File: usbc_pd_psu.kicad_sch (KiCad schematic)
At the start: 35 parts, among them J1 USB-C 5 A, J2 OUTPUT, J3 PROG, Q1 AON6324, Q2 AON6324, Q3 AON6324, Q4 AON6324, Q5 TIP120, U1 CH224K, U2 IR2104, U3 IR2104, U4 LM358, U5 LP2950-5.0, U6 CH32V003F4P6

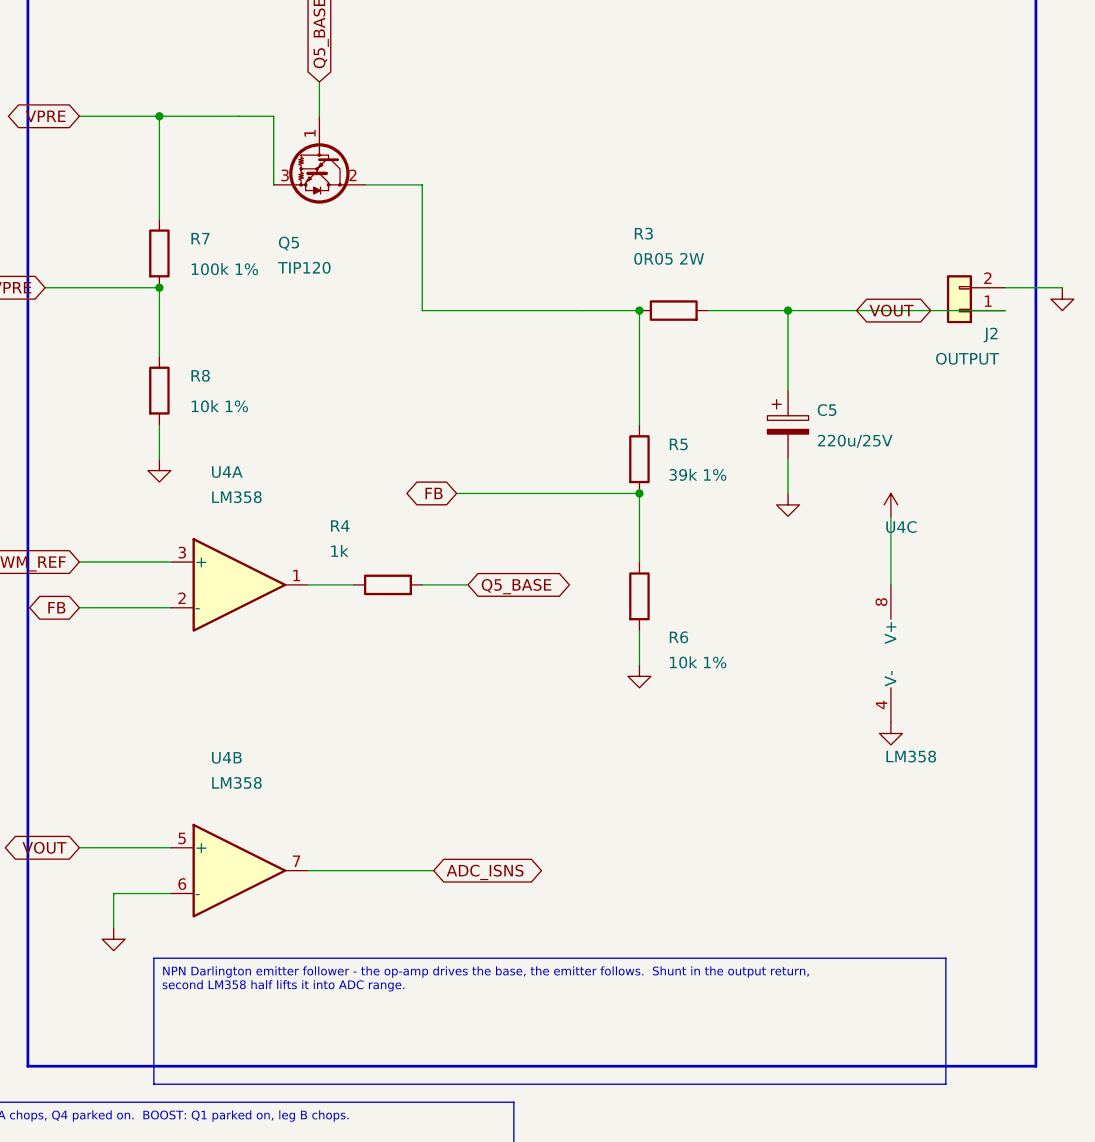
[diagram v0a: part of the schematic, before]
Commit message: v0.4: turn the pass device round to a PNP
The NPN follower cannot reach the top of the range.  Its base has to sit two
Vbe above the output, and the op-amp driving it runs from the same
pre-regulator rail as the pass device itself, so once the output climbs the
amplifier saturates before the base gets high enough.  The supply simply
stops following the setpoint near full scale.

Turning the device round fixes it: a TIP127 PNP Darlington SINKS base current
instead of sourcing it, so the stage needs no headroom above VOUT at all and
the pre-regulator only has to stay a dropout above the output.

Everything else on the sheet is unchanged - same MCU, same buck-boost, same
shunt in the output return.
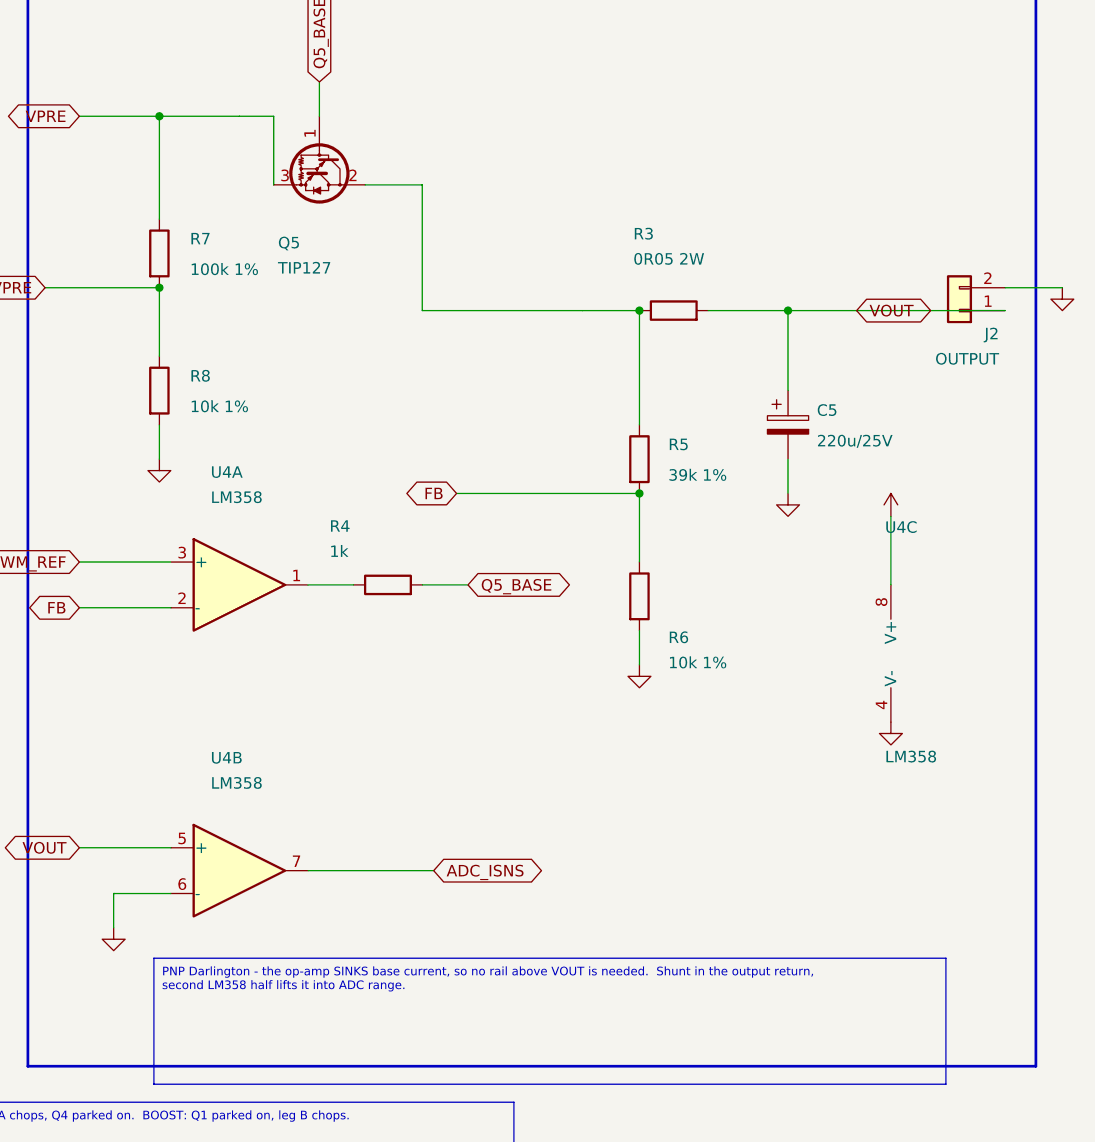
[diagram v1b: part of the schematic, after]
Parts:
- removed Q5: TIP120, Package_TO_SOT_THT:TO-220-3_Vertical, symbol Transistor_BJT:TIP120
- added Q5: TIP127, Package_TO_SOT_THT:TO-220-3_Vertical, symbol Transistor_BJT:TIP127
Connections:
- net Q5_BASE: now also Q5.1 (B)
- net VPRE: now also Q5.3 (E)
- net at R3.1, R5.1: now also Q5.2 (C)

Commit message: v0.5: add the front panel, and the MCU it needs
OLED, rotary encoder with its push, three keys and three indicator lamps.

Adding the panel needs eleven more pins and only two were left, so the MCU
moves up to a CH32V203C8T6.  Same RISC-V family, same toolchain, same
programming header - forty-eight pins instead of twenty, of which thirty-seven
are usable.  Nothing else on the sheet changes.

Choosing within the family rather than switching vendor keeps the existing
firmware work and the WCH-LinkE probe usable, which matters more at this stage
than the price difference.
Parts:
- removed U6: CH32V003F4P6, Package_SO:TSSOP-20_4.4x6.5mm_P0.65mm, symbol MCU_WCH_CH32V0:CH32V003FxPx
- added C9: 100nF, Capacitor_SMD:C_0805_2012Metric, symbol Device:C
- added D4: red, LED_SMD:LED_0805_2012Metric, symbol Device:LED
- added D5: amber, LED_SMD:LED_0805_2012Metric, symbol Device:LED
- added D6: green, LED_SMD:LED_0805_2012Metric, symbol Device:LED
- added J4: OLED 0.96in I2C, Connector_PinHeader_2.54mm:PinHeader_1x04_P2.54mm_Vertical, symbol Connector_Generic:Conn_01x04
- added R10, R9: 10k, Resistor_SMD:R_0805_2012Metric, symbol Device:R
- added R11, R12, R13: 1k, Resistor_SMD:R_0805_2012Metric, symbol Device:R
- added SW1: EC11, Rotary_Encoder:RotaryEncoder_Alps_EC11E-Switch_Vertical_H20mm, symbol Device:RotaryEncoder_Switch
- added SW2: OUTPUT, Button_Switch_SMD:SW_SPST_B3S-1000, symbol Switch:SW_Push
- added SW3: SELECT, Button_Switch_SMD:SW_SPST_B3S-1000, symbol Switch:SW_Push
- added SW4: BACK, Button_Switch_SMD:SW_SPST_B3S-1000, symbol Switch:SW_Push
- added U6: CH32V203C8T6, Package_QFP:LQFP-48_7x7mm_P0.5mm, symbol MCU_WCH_CH32V2:CH32V203CxTx
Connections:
- net +5V: now also C9.2, D4.2 (A), D5.2 (A), D6.2 (A), J4.1 (Pin_1), J4.2 (Pin_2), R10.2, R9.1, SW1.C, SW1.S2, SW2.1, SW3.1, SW4.1, U6.1 (VBAT), U6.23 (VSS), U6.24 (VDD_VIO), U6.35 (VSS), U6.36 (VDD), U6.47 (VSS), U6.48 (VDD), U6.8 (VSSA), U6.9 (VDDA)
- net ADC_ISNS: now also U6.14 (PA4)
- net ADC_VBUS: now also U6.10 (PA0)
- net ADC_VPRE: now also U6.11 (PA1)
- net CFG1: now also U6.20 (PB2)
- net CFG2: now also U6.21 (PB10)
- net CFG3: now also U6.22 (PB11)
- net EN_A: now also U6.31 (PA10)
- net EN_B: now also U6.32 (PA11)
- net PD_PG: now also U6.19 (PB1)
- net PWM_A: now also U6.29 (PA8)
- net PWM_B: now also U6.30 (PA9)
- net PWM_REF: now also U6.15 (PA5)
- net UART_RX: now also U6.43 (PB7); no longer J3.3 (Pin_3)
- net UART_TX: now also J3.3 (Pin_3), U6.42 (PB6); no longer J3.2 (Pin_2)
- net SWIO renamed SWDIO
- net SWDIO: now also U6.34 (SWDIO)
- new net: R10.1, U6.44 (BOOT0)
- new net: D6.1 (K), R13.1
- new net: C9.1, R9.2, U6.7 (~{RST})
- new net: D4.1 (K), R11.1
- new net: D5.1 (K), R12.1
- new net BTN_BACK: SW4.2, U6.4 (PC15)
- new net BTN_OUT: SW2.2, U6.2 (PC13)
- new net BTN_SEL: SW3.2, U6.3 (PC14)
- new net ENC_A: SW1.A, U6.25 (PB12)
- new net ENC_B: SW1.B, U6.26 (PB13)
- new net ENC_SW: SW1.S1, U6.27 (PB14)
- new net I2C_SCL: J4.3 (Pin_3), U6.45 (PB8)
- new net I2C_SDA: J4.4 (Pin_4), U6.46 (PB9)
- new net LED_CC: R12.2, U6.39 (PB3)
- new net LED_HB: R13.2, U6.40 (PB4)
- new net LED_OUT: R11.2, U6.38 (PA15)
- new net SWCLK: J3.2 (Pin_2), U6.37 (SWCLK)
- no-connect marks 4 -> 12
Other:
- note added: "7 - USER INTERFACE"

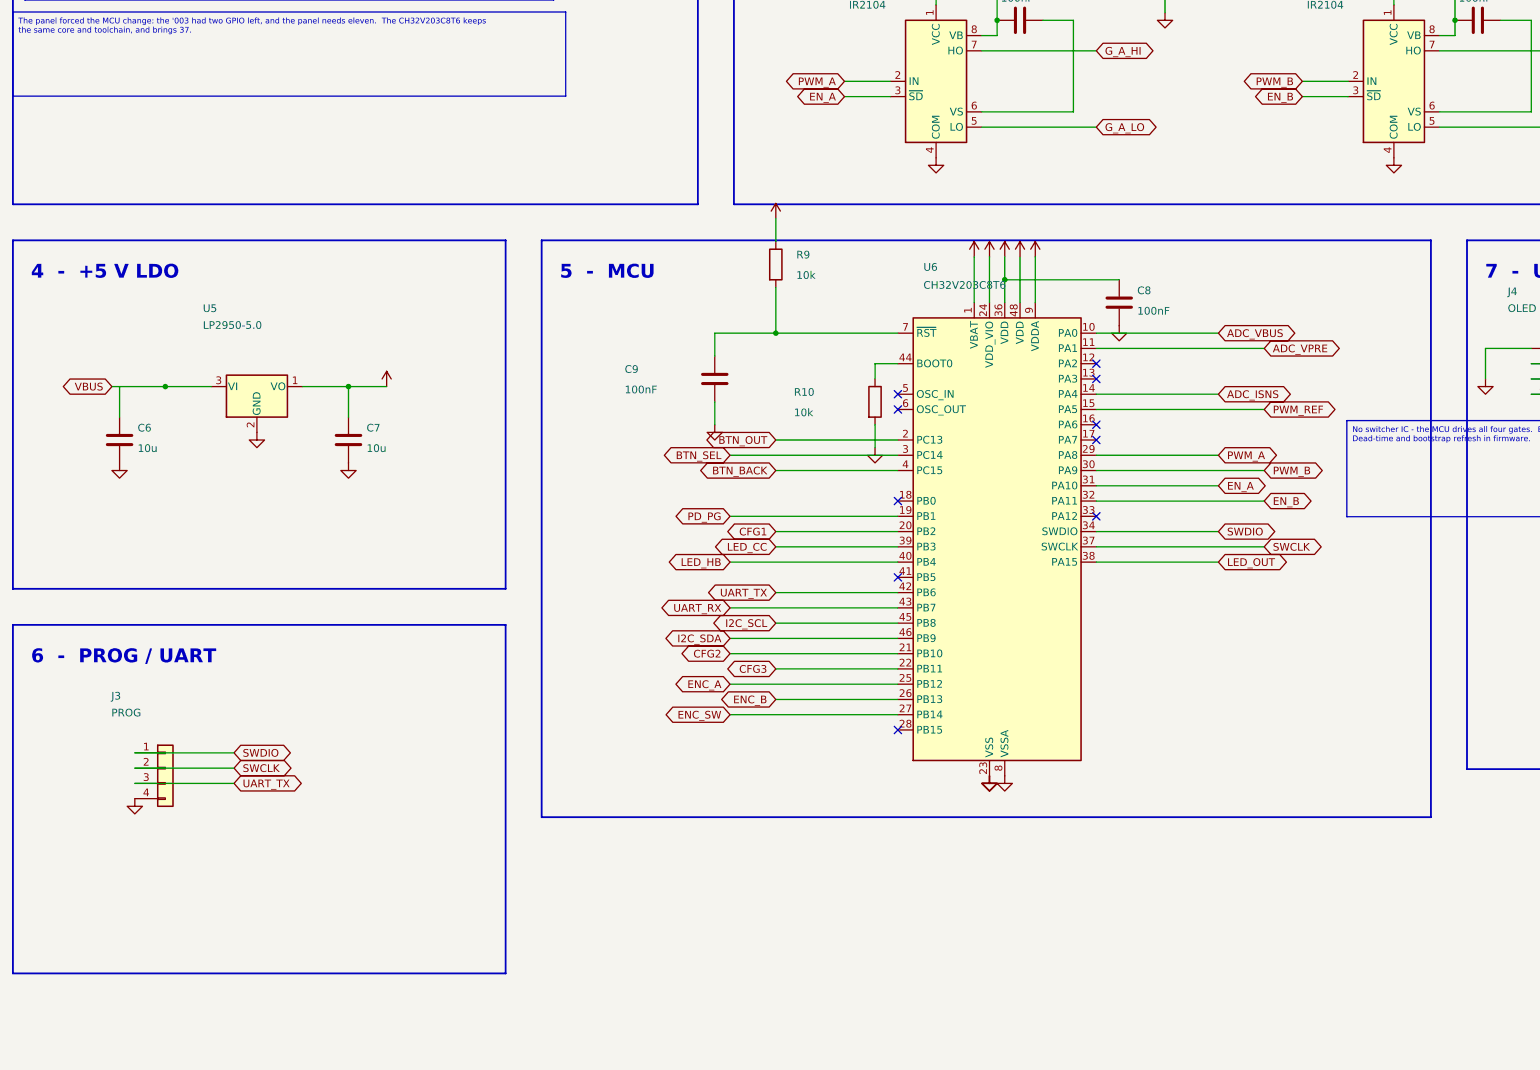
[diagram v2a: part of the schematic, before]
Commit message: v0.6: hardware over-current trip
A comparator watches the sense amplifier and pulls the driver enable low
directly.

Bench testing with a deliberate short showed the firmware loop cannot react in
time: by the time a 5 kHz loop notices, the FETs have already taken the
current.  The trip has to be hardware, and it has to bypass the MCU entirely.

This is also where the single-sheet layout runs out of room.  Everything still
fits, but only just, and the next thing added will not.
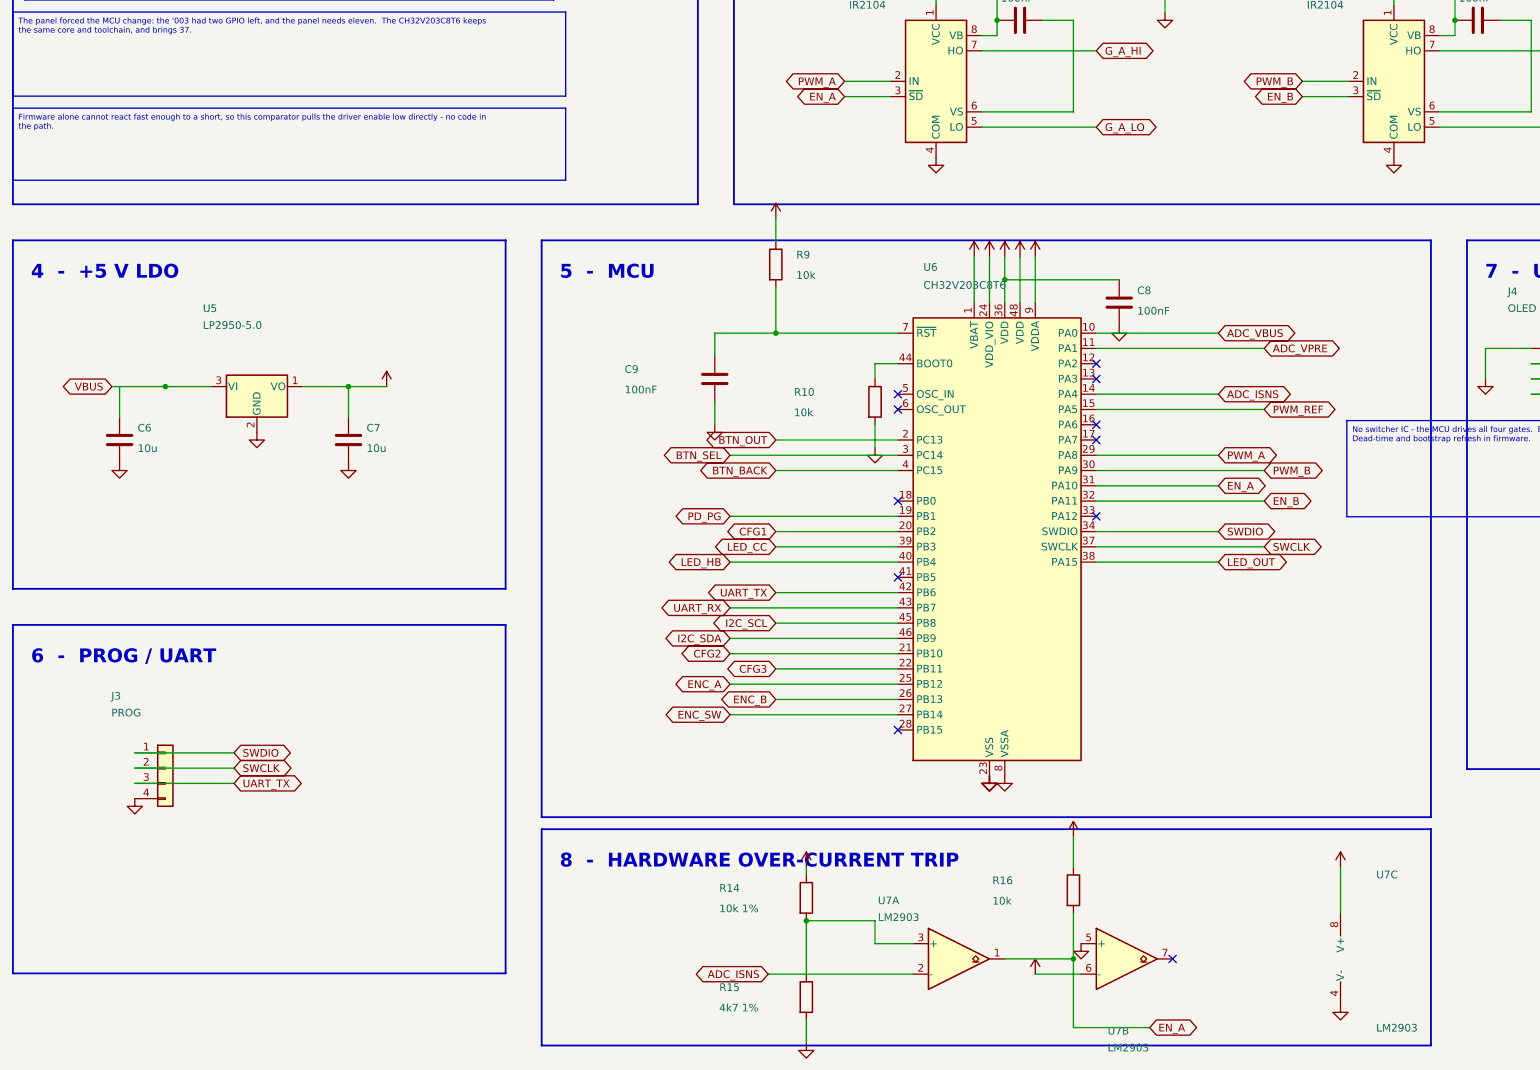
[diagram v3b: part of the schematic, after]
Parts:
- added R14: 10k 1%, Resistor_SMD:R_0805_2012Metric, symbol Device:R
- added R15: 4k7 1%, Resistor_SMD:R_0805_2012Metric, symbol Device:R
- added R16: 10k, Resistor_SMD:R_0805_2012Metric, symbol Device:R
- added U7: LM2903, Package_SO:SOIC-8_3.9x4.9mm_P1.27mm, symbol Comparator:LM2903
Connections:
- net +5V: now also R14.1, R15.2, R16.1, U7.4 (V-), U7.5 (+), U7.6 (-), U7.8 (V+)
- net ADC_ISNS: now also R14.2, R15.1, U7.2 (-), U7.3 (+)
- net EN_A: now also R16.2, U7.1
- no-connect marks 12 -> 13
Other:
- note added: "8 - HARDWARE OVER-CURRENT TRIP"
